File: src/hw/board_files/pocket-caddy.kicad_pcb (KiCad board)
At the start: 4 copper layers, 100 x 100 mm, 100 parts, among them J1 Conn_01x03_Pin, J2 Conn_01x03_Pin, J3 Conn_01x03_Pin, J4 Test_Points, J5 Molex 104031-0811, J6 Screw_Terminal_01x03, P1 USB_C_Plug_USB2.0, Q1 PMOS, SW1 SW_PWR, SW2 RESET, SW3 BTN_2, SW4 BTN_1_BOOT, SW5 BTN_3, U1 FT234XD-R, U2 MCP73871, U3 TPS63031DSKR, U4 ESP32-C3-WROOM-02, U5 NHD-C0220BIZ-FSRGB, U6 NEO-M9N, U7 BQ27427, U8 SHT30-DIS, Y1 32.768kHz

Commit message: Lots of layout progress, changed some references (need to update BOM)
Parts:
- removed the C18 at (72.8, 130.4)
- removed the C19 at (77.6, 130.2)
- removed the C22 at (50.6, 82.5)
- removed the C23 at (114.4, 93.2)
- removed the J2 at (74.1, 84.8)
- removed the J3 at (57.9, 84.8)
- removed JP3: SolderJumper_Open, Jumper:SolderJumper-2_P1.3mm_Open_TrianglePad1.0x1.5mm
- removed P1: USB_C_Plug_USB2.0, Connector_USB:USB_C_Receptacle_GCT_USB4110
- removed the R18 at (87.6, 81.1)
- removed the R20 at (112.8, 93.2)
- removed the U5 at (78.7, 112.3)
- removed U8: SHT30-DIS, Sensor_Humidity:Sensirion_DFN-8-1EP_2.5x2.5mm_P0.5mm_EP1.1x1.7mm
- added C20: 100n, Capacitor_SMD:C_0603_1608Metric_Pad1.08x0.95mm_HandSolder, F.Cu at (-38.4, 111.6)
- added C21: 100n, Capacitor_SMD:C_0603_1608Metric_Pad1.08x0.95mm_HandSolder, F.Cu at (-38.4, 114.1)
- added J1: USB_C_Receptacle_USB2.0_14P, Connector_USB:USB_C_Receptacle_GCT_USB4105-xx-A_16P_TopMnt_Horizontal, F.Cu at (163.7, 87.0)
- added J4: Conn_01x03_Pin, Connector_PinHeader_2.54mm:PinHeader_1x03_P2.54mm_Vertical, F.Cu at (-49.5, 122.7)
- added J5: Conn_01x03_Pin, Connector_PinHeader_2.54mm:PinHeader_1x03_P2.54mm_Vertical, F.Cu at (-44.9, 122.7)
- added J7: Conn_01x04, Connector_PinSocket_2.54mm:PinSocket_1x04_P2.54mm_Vertical, F.Cu at (183.3, 101.0)
- added JP1: SolderJumper_Open, Jumper:SolderJumper-2_P1.3mm_Open_TrianglePad1.0x1.5mm, F.Cu at (-49.6, 131.8)
- added R19: 10k, Resistor_SMD:R_0603_1608Metric_Pad0.98x0.95mm_HandSolder, F.Cu at (-38.4, 116.6)
- added R21: 10k, Resistor_SMD:R_0603_1608Metric_Pad0.98x0.95mm_HandSolder, F.Cu at (-38.4, 119.2)
- added R5: 5k1, Resistor_SMD:R_0603_1608Metric_Pad0.98x0.95mm_HandSolder, F.Cu at (170.8, 89.5)
- added U7: SHT30-DIS, Sensor_Humidity:Sensirion_DFN-8-1EP_2.5x2.5mm_P0.5mm_EP1.1x1.7mm, F.Cu at (-61.1, 149.0)
- BT2: moved to B.Cu
- J8: renamed from J5; moved to B.Cu
- moved H1 343.5 mm to (-29.1, 187.1)
- moved H2 343.5 mm to (-29.1, 195.0)
- moved NT1 286.0 mm to (271.4, 73.7), turned to 0 degrees
- moved J3 228.3 mm to (227.1, 73.7), turned to -90 degrees
- moved BT2 213.3 mm to (-61.1, 198.1)
- moved C3 197.8 mm to (246.3, 55.9)
- moved C4 197.8 mm to (244.5, 55.9)
- moved U6 197.8 mm to (245.5, 59.5)
- moved C22 197.8 mm to (242.7, 59.5)
- moved C23 197.8 mm to (242.7, 55.9)
- moved R20 197.8 mm to (249.7, 60.5)
- moved R22 197.8 mm to (249.7, 58.7)
- moved C2 171.0 mm to (210.1, 108.6), turned to -90 degrees
- moved C5 170.8 mm to (236.1, 71.3)
- moved C6 170.8 mm to (238.7, 71.3)
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- renumbered C20 to C18, C21 to C19, C24 to C22, C25 to C23, J6 to J2, J1 to J3, J4 to J6, R9 to R10, R10 to R11, R11 to R12, R12 to R13, R13 to R14, R14 to R15, R15 to R16, R16 to R17, R17 to R18, R19 to R20, R21 to R22, R5 to R6, R6 to R7, R7 to R8, R8 to R9, U6 to U5, U7 to U6
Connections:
- net Net-(D1-I/O1) renamed /USB-C and Power/USB0_D+
- net Net-(D1-I/O2) renamed /USB-C and Power/USB0_D-
- J2 pad 1: VBAT -> /USB-C and Power/NTC_THERM
- J2 pad 3: /USB-C and Power/NTC_THERM -> VBAT
- JP2 pad 1: /Microcontroller/USB_D- -> /Microcontroller/USB_D+
- U4 pad 13: Net-(JP2-B) -> Net-(JP1-B)
- U4 pad 14: Net-(JP3-B) -> Net-(JP2-B)
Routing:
- net GND: track 72.2 -> 7.35 mm, vias 23 -> 10
- net /SPI_SCK: track 0.60 -> 18.9 mm, vias 0 -> 1
- net /SPI_MOSI: track 0.00 -> 16.4 mm, vias 0 -> 1
- net /SCL: track 4.87 -> 20.8 mm
- net /SPI_MISO: track 0.65 -> 16.4 mm, vias 0 -> 1
- net /SDA: track 4.77 -> 17.2 mm
- net Net-(U1-3V3OUT): track 0.00 -> 9.76 mm, vias 0 -> 2
- net Net-(U4-EN): track 14.9 -> 6.56 mm
- net /Microcontroller/BTN_2: track 10.3 -> 3.32 mm
- net /Microcontroller/BTN_1_BOOT: track 10.3 -> 3.32 mm
- net /Microcontroller/BTN_3: track 10.3 -> 3.32 mm
- net (no net): track 6.26 -> 0.00 mm
- net +3V3: track 34.4 -> 28.5 mm, vias 12 -> 7
- net V_USB: track 4.31 -> 10.0 mm
- net V_BCKP: track 4.78 -> 0.00 mm
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- added copper zone on F.Cu, net VBAT
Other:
- outline, holes or cut-outs redrawn
- board text added: "1"
- board text added: "2"
- board text added: "3"
- board text added: "Figure out how to use net tie."
- board text removed: "Coin Cell Battery"
- board text removed: "GND"
- board text removed: "Li-Po Battery"
- board text removed: "V_BCKP"

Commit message: Layout updates
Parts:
- JP1, JP2: moved to B.Cu
- moved JP1 229.7 mm to (175.9, 88.5), turned to -90 degrees
- moved JP2 226.4 mm to (171.5, 86.8), turned to -90 degrees
- moved J4 197.5 mm to (144.6, 86.0)
- moved J5 197.5 mm to (149.1, 86.0)
- moved C2 27.4 mm to (236.6, 101.3)
- moved D3 27.4 mm to (229.7, 101.7)
- moved J2 27.4 mm to (242.6, 101.2)
- moved R10 27.4 mm to (229.9, 99.7)
- moved R12 27.4 mm to (229.9, 95.7)
- moved R7 27.4 mm to (234.6, 101.0)
- moved R8 27.4 mm to (232.9, 101.0)
- moved R9 27.4 mm to (229.9, 91.7)
- moved U2 27.4 mm to (235.0, 95.7)
- moved D2 27.4 mm to (229.7, 93.7)
- moved D4 27.4 mm to (229.7, 97.7)
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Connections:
- R1 pad 1: +5V -> +3V3
- R4 pad 2: +5V -> +3V3
- U1 pad 4: +5V -> +3V3
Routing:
- net /SCL: track 20.8 -> 6.93 mm
- net Net-(AE1-FEED): track 15.1 -> 1.74 mm
- net /USB-C and Power/USB0_D+: track 2.75 -> 13.3 mm
- net /SDA: track 17.2 -> 6.76 mm
- net /USB-C and Power/USB0_D-: track 2.73 -> 12.7 mm, vias 0 -> 2
- net Net-(U1-3V3OUT): track 9.76 -> 1.46 mm, vias 2 -> 1
- net V_USB: track 10.0 -> 17.1 mm
- net Net-(U1-CBUS0): track 0.00 -> 6.32 mm
- net Net-(U1-~{RESET}): track 0.00 -> 3.04 mm
- net /Microcontroller/USB_D+: track 4.52 -> 2.09 mm
- net /Microcontroller/USB_D-: track 4.54 -> 2.10 mm
- net +5V: track 1.46 -> 0.00 mm, vias 1 -> 0
- net +3V3: track 28.5 -> 29.9 mm, vias 7 -> 8
- net GND: vias 10 -> 11

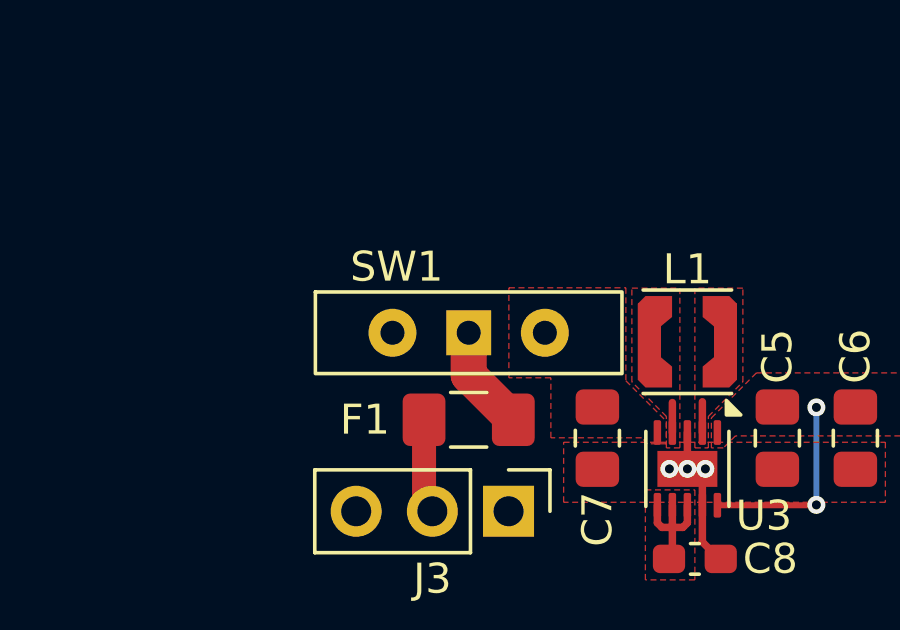
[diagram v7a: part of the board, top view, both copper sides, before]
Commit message: Added 3D model for power switch
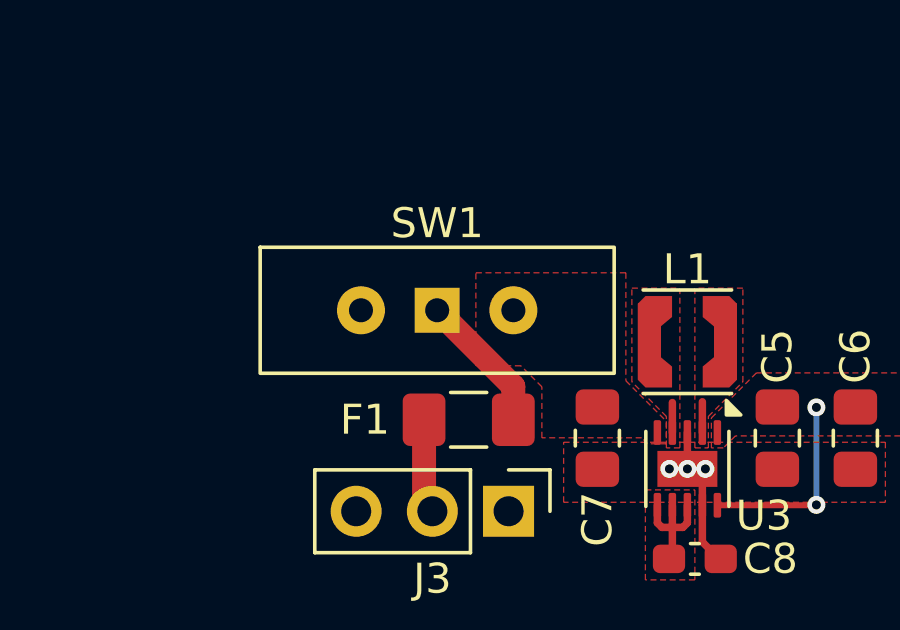
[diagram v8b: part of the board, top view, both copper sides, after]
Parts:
- moved SW1 1.29 mm to (224.8, 67.0)
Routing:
- net Net-(SW1-B): track 3.52 -> 4.70 mm
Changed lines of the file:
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@@
 	(footprint "Button_Switch_THT:SW_Slide-03_Wuerth-WS-SLTV_10x2.5x6.4_P2.54mm"
 		(layer "F.Cu")
-		(at 225.81 67.75)
+		(at 224.76 67)
 		(descr "Wuerth, WS-SLTV, 450301014042, https://www.we-online.com/components/products/datasheet/450301014042.pdf")
 		(tags "switch single-pole opposite-side-connection double-throw SPDT würth wurth")
 		(property "Reference" "SW1"
-			(at -2.4 -2.2 0)
+			(at 0 -2.9 0)
 			(layer "F.SilkS")
 			(effects
@@
 		)
 		(property "Value" "SW_PWR"
-			(at 0 3.81 0)
+			(at 0 4.4 0)
 			(layer "F.Fab")
 			(effects
@@
 		(attr through_hole)
 		(fp_rect
-			(start -5.11 -1.36)
-			(end 5.11 1.36)
+			(start -5.9 -2.1)
+			(end 5.9 2.1)
 			(stroke
 				(width 0.12)
-				(type default)
+				(type solid)
 			)
 			(fill no)
@@
 		)
 		(fp_rect
-			(start -5.25 -1.5)
-			(end 5.25 1.5)
+			(start -6 -2.2)
+			(end 6 2.2)
 			(stroke
 				(width 0.05)
-				(type default)
+				(type solid)
 			)
 			(fill no)
@@
 		)
 		(fp_rect
-			(start -5 -1.25)
-			(end 5 1.25)
+			(start -5.8 -2)
+			(end 5.8 2)
 			(stroke
 				(width 0.1)
-				(type default)
+				(type solid)
 			)
 			(fill no)
@@
 		)
 		(fp_text user "${REFERENCE}"
-			(at 0 2.54 0)
+			(at 0 3.13 0)
 			(layer "F.Fab")
 			(effects
@@
 			)
 		)
+		(model "${KIPRJMOD}/3d_models/141_EG1218.stp"
+			(offset
+				(xyz 0 0 0)
+			)
+			(scale
+				(xyz 1 1 1)
+			)
+			(rotate
+				(xyz 0 0 0)
+			)
+		)
 	)
 	(footprint "MountingHole:MountingHole_3.2mm_M3_Pad"
@@
 	)
 	(segment
-		(start 225.81 67.75)
-		(end 225.81 69.1625)
-		(width 1.2)
+		(start 227.2975 70.65)
+		(end 227.2975 69.5375)
+		(width 0.8)
 		(layer "F.Cu")
 		(net 21)
 	)
 	(segment
-		(start 225.81 69.1625)
-		(end 227.2975 70.65)
-		(width 1.2)
+		(start 227.2975 69.5375)
+		(end 224.76 67)
+		(width 0.8)
 		(layer "F.Cu")
 		(net 21)
@@
 	)
 	(zone
+		(net 51)
+		(net_name "Net-(U5-RF_IN)")
+		(layer "F.Cu")
+		(name "$teardrop_padvia$")
+		(hatch none 0.1)
+		(priority 30001)
+		(attr
+			(teardrop
+				(type padvia)
+			)
+		)
+		(connect_pads yes
+			(clearance 0)
+		)
+		(min_thickness 0.0254)
+		(filled_areas_thickness no)
+		(fill yes
+			(thermal_gap 0.5)
+			(thermal_bridge_width 0.5)
+			(island_removal_mode 1)
+			(island_area_min 10)
+		)
+		(polygon
+			(pts
+				(xy 184.92175 83.65) (xy 185.07825 83.65) (xy 185.456921 83.028387) (xy 185 82.649) (xy 184.543079 83.028387)
+			)
+		)
+	)
+	(zone
 		(net 8)
 		(net_name "PGND")
@@
 	)
 	(zone
-		(net 51)
-		(net_name "Net-(U5-RF_IN)")
-		(layer "F.Cu")
-		(name "$teardrop_padvia$")
-		(hatch none 0.1)
-		(priority 30001)
-		(attr
-			(teardrop
-				(type padvia)
-			)
-		)
-		(connect_pads yes
-			(clearance 0)
-		)
-		(min_thickness 0.0254)
-		(filled_areas_thickness no)
-		(fill yes
-			(thermal_gap 0.5)
-			(thermal_bridge_width 0.5)
-			(island_removal_mode 1)
-			(island_area_min 10)
-		)
-		(polygon
-			(pts
-				(xy 185.07825 83.9) (xy 184.92175 83.9) (xy 184.615224 84.423463) (xy 185 85.201) (xy 185.384776 84.423463)
-			)
-		)
-	)
-	(zone
-		(net 51)
-		(net_name "Net-(U5-RF_IN)")
+		(net 7)
+		(net_name "+3V3")
 		(layer "F.Cu")
-		(name "$teardrop_padvia$")
-		(hatch none 0.1)
-		(priority 30003)
-		(attr
-			(teardrop
-				(type padvia)
-			)
-		)
+		(hatch edge 0.5)
+		(priority 2)
 		(connect_pads yes
-			(clearance 0)
+			(clearance 0.25)
 		)
-		(min_thickness 0.0254)
+		(min_thickness 0.25)
 		(filled_areas_thickness no)
 		(fill yes
 			(thermal_gap 0.5)
 			(thermal_bridge_width 0.5)
-			(island_removal_mode 1)
-			(island_area_min 10)
+			(smoothing fillet)
+			(radius 0.2)
 		)
 		(polygon
 			(pts
-				(xy 184.92175 83.65) (xy 185.07825 83.65) (xy 185.456921 83.028387) (xy 185 82.649) (xy 184.543079 83.028387)
+				(xy 233.9 71.5875) (xy 233.9 70.5875) (xy 235.4 69.0875) (xy 241.8 69.0875) (xy 241.8 71.1875) (xy 234.7 71.1875)
+				(xy 234.3 71.5875)
 			)
 		)
 	)
 	(zone
-		(net 7)
-		(net_name "+3V3")
+		(net 9)
+		(net_name "Net-(SW1-A)")
 		(layer "F.Cu")
 		(hatch edge 0.5)
-		(priority 2)
+		(priority 3)
 		(connect_pads yes
 			(clearance 0.25)
@@
 		(polygon
 			(pts
-				(xy 233.9 71.5875) (xy 233.9 70.5875) (xy 235.4 69.0875) (xy 241.8 69.0875) (xy 241.8 71.1875) (xy 234.7 71.1875)
-				(xy 234.3 71.5875)
+				(xy 226.05 65.75) (xy 231.05 65.75) (xy 231.05 69.35) (xy 232.4 70.7) (xy 232.4 71.45) (xy 231.775 71.45)
+				(xy 231.575 71.25) (xy 228.25 71.25) (xy 228.25 69.55) (xy 227.55 68.85) (xy 226.05 68.85)
 			)
 		)
 	)
 	(zone
-		(net 9)
-		(net_name "Net-(SW1-A)")
+		(net 51)
+		(net_name "Net-(U5-RF_IN)")
 		(layer "F.Cu")
-		(hatch edge 0.5)
-		(priority 3)
+		(name "$teardrop_padvia$")
+		(hatch none 0.1)
+		(priority 30000)
+		(attr
+			(teardrop
+				(type padvia)
+			)
+		)
 		(connect_pads yes
-			(clearance 0.25)
+			(clearance 0)
 		)
-		(min_thickness 0.25)
+		(min_thickness 0.0254)
 		(filled_areas_thickness no)
 		(fill yes
 			(thermal_gap 0.5)
 			(thermal_bridge_width 0.5)
-			(smoothing fillet)
-			(radius 0.2)
+			(island_removal_mode 1)
+			(island_area_min 10)
 		)
 		(polygon
 			(pts
-				(xy 227.15 66.25) (xy 231.05 66.25) (xy 231.05 69.35) (xy 232.4 70.7) (xy 232.4 71.45) (xy 231.775 71.45)
-				(xy 231.575 71.25) (xy 228.55 71.25) (xy 228.55 69.25) (xy 227.15 69.25)
+				(xy 185.07825 83.9) (xy 184.92175 83.9) (xy 184.615224 84.423463) (xy 185 85.201) (xy 185.384776 84.423463)
 			)
 		)
@@
 	)
 	(zone
-		(net 28)
-		(net_name "/SPI_SCK")
+		(net 26)
+		(net_name "/SPI_MISO")
 		(layer "B.Cu")
 		(name "$teardrop_padvia$")
 		(hatch none 0.1)
-		(priority 30002)
+		(priority 30001)
 		(attr
 			(teardrop
@@
 		(polygon
 			(pts
-				(xy 174.72 127.4375) (xy 174.47 127.4375) (xy 174.17 127.8625) (xy 174.595 128.4135) (xy 175.02 127.8625)
+				(xy 176.92 127.4375) (xy 176.67 127.4375) (xy 176.37 127.8625) (xy 176.795 128.4135) (xy 177.22 127.8625)
 			)
 		)
@@
 	)
 	(zone
-		(net 26)
-		(net_name "/SPI_MISO")
+		(net 28)
+		(net_name "/SPI_SCK")
 		(layer "B.Cu")
 		(name "$teardrop_padvia$")
 		(hatch none 0.1)
-		(priority 30001)
+		(priority 30002)
 		(attr
 			(teardrop
@@
 		(polygon
 			(pts
-				(xy 176.92 127.4375) (xy 176.67 127.4375) (xy 176.37 127.8625) (xy 176.795 128.4135) (xy 177.22 127.8625)
+				(xy 174.72 127.4375) (xy 174.47 127.4375) (xy 174.17 127.8625) (xy 174.595 128.4135) (xy 175.02 127.8625)
 			)
 		)
